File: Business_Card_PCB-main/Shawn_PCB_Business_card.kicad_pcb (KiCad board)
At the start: 2 copper layers, 86.6 x 54.7 mm, 28 parts, among them U1 NT3H1101W0FHKH

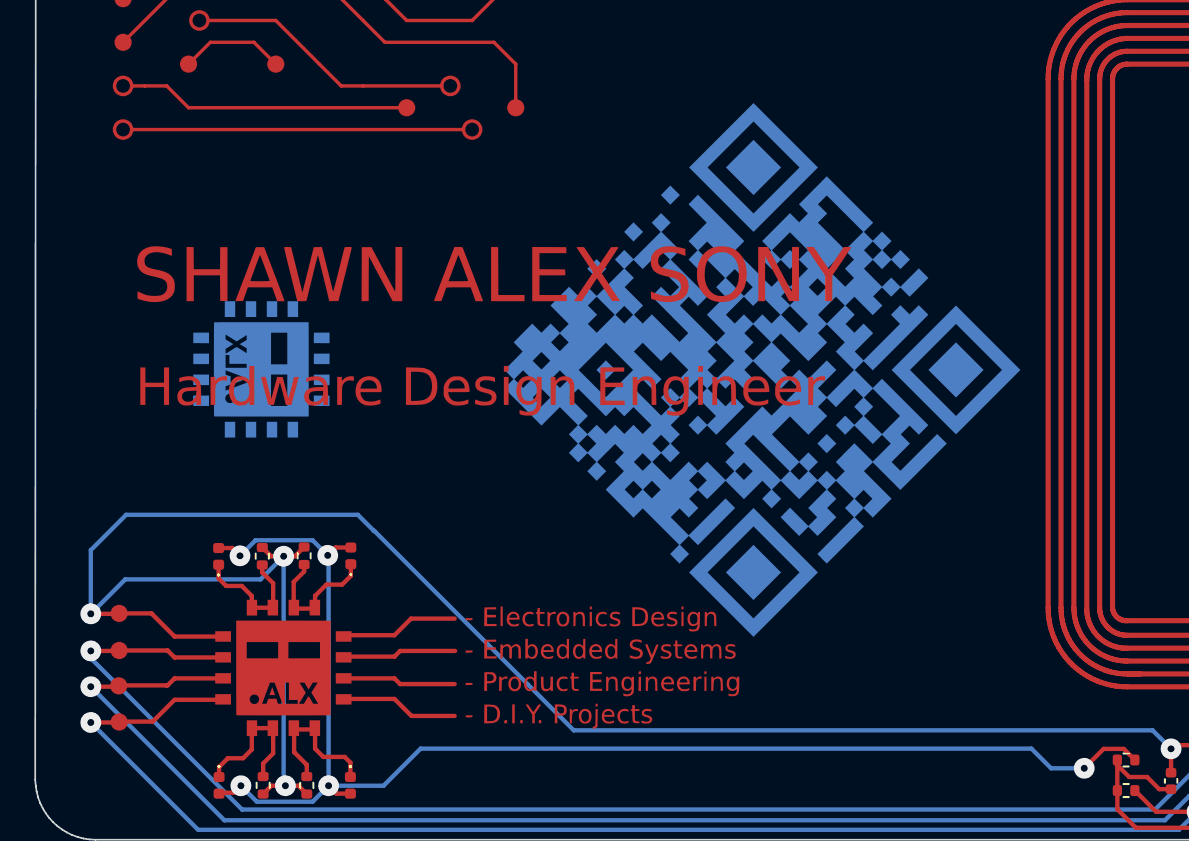
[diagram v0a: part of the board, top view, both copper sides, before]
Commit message: added my name and redesigned the PCB logo thing
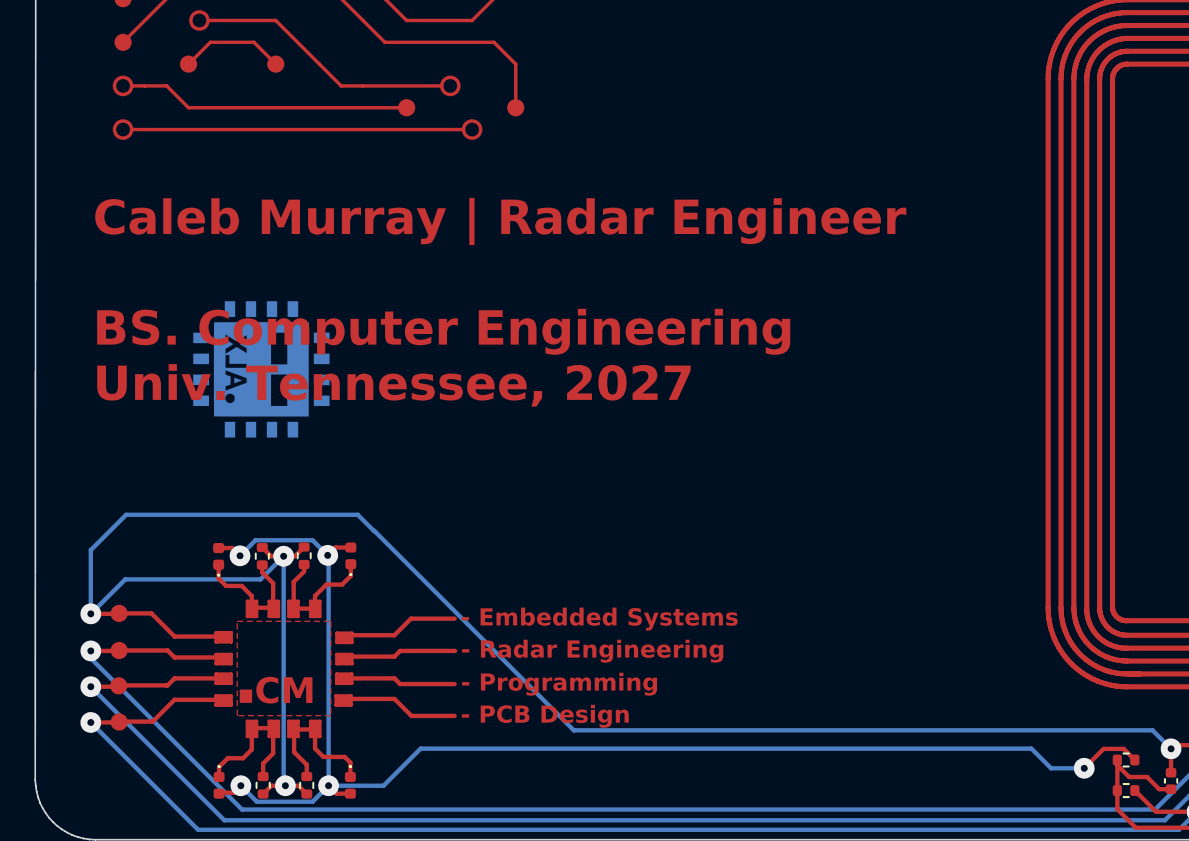
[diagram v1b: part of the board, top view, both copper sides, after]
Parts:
- removed the G*** at (148.2, 69.5) (x2)
- removed the G*** at (148.5, 70.5) (x2)
- removed the G*** at (121.1, 87.9) (x2)
- moved G*** 2.40 mm to (152.0, 71.2)
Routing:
- added copper zone on F.Cu, net (none)
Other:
- board text added: "- Embedded Systems"
- board text added: "- PCB Design"
- board text added: "- Programming"
- board text added: "- Radar Engineering"
- board text added: "."
- board text added: "CM"
- board text added: "Caleb Murray | Radar Engineer BS. Computer Engineering Univ. Tennessee, 2027"

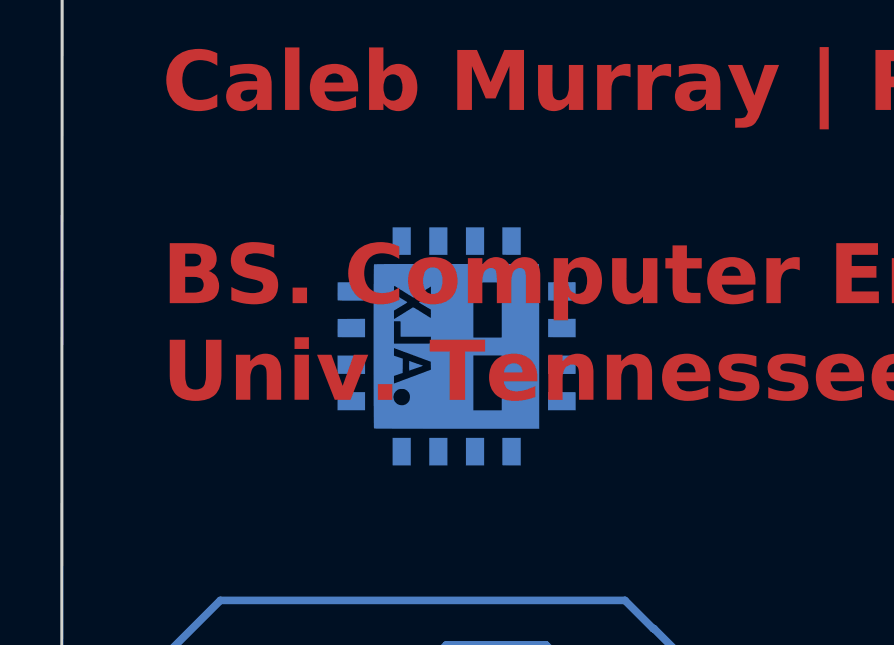
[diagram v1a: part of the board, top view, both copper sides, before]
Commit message: updated back text
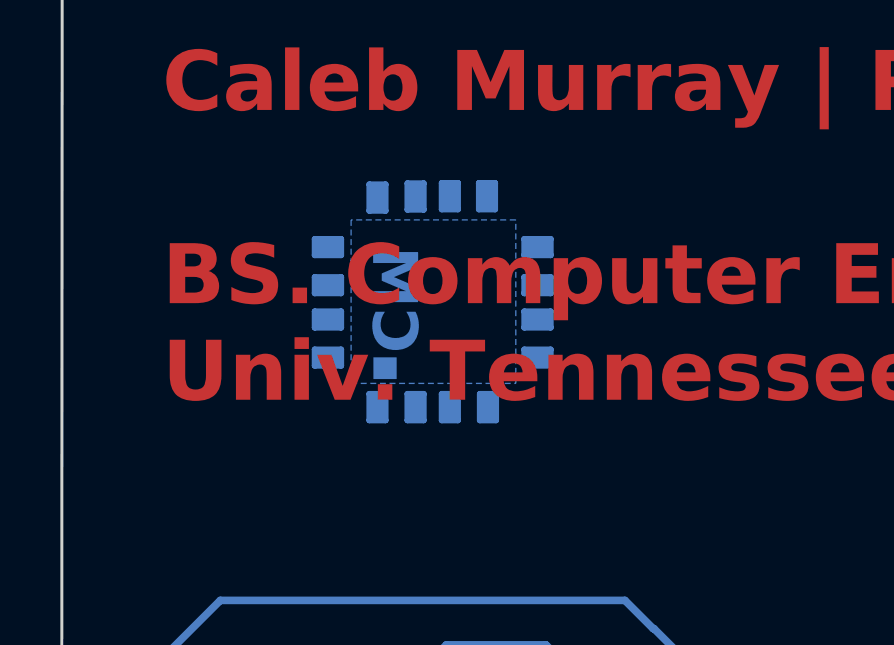
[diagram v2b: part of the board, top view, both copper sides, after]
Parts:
- removed the G*** at (119.8, 70.5) (x2)
- removed the G*** at (152.0, 71.2)
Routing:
- added copper zone on B.Cu, net (none)
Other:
- board text added: "> root@caleb.cm:~$ cat Hello.txt > ----------------------- Hey! I'm Caleb! It's nice to meet you. Scan the card to connect. ----------------------- > root@caleb.cm:~$"

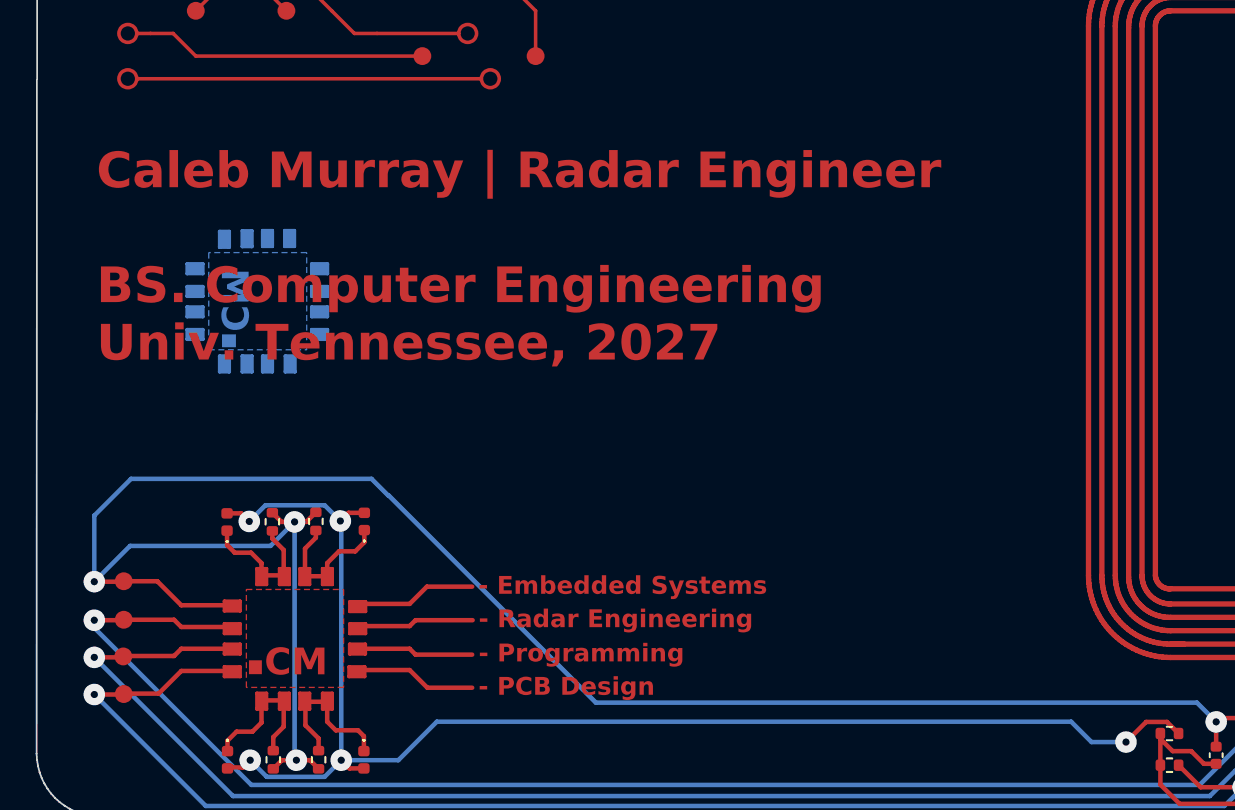
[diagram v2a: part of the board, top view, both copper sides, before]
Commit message: fixed soldermask everywhere
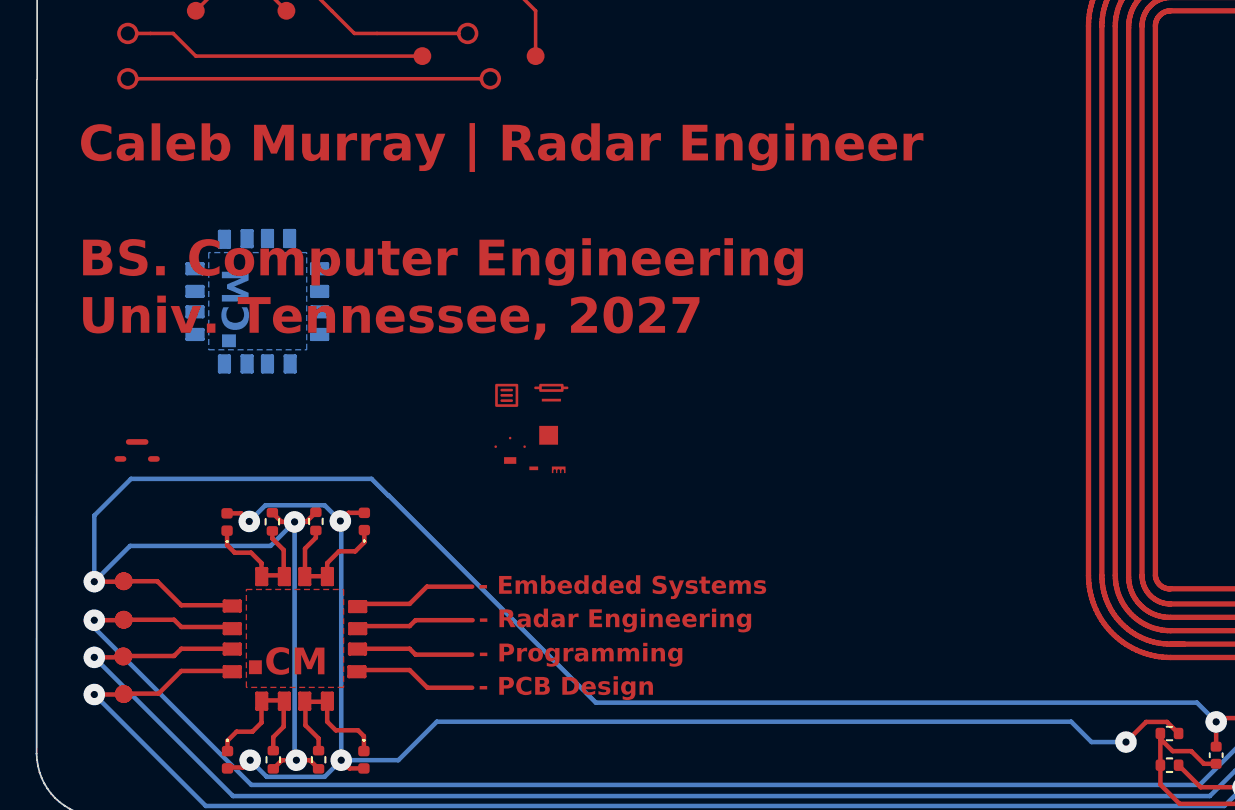
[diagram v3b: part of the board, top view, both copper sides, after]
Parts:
- added TP1: TestPoint, TestPoint:TestPoint_Pad_D1.0mm, F.Cu at (111.5, 86.8)
- added TP2: TestPoint, TestPoint:TestPoint_Pad_D1.0mm, F.Cu at (111.5, 88.9)
- added TP4: TestPoint, TestPoint:TestPoint_Pad_D1.0mm, F.Cu at (111.5, 91.0)
- added TP5: TestPoint, TestPoint:TestPoint_Pad_D1.0mm, F.Cu at (111.5, 84.7)
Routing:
- net (no net): track 26.9 -> 53.8 mm
- net GND: track 119.4 -> 133.6 mm
- net Net-(D1-Pad1): track 8.61 -> 17.2 mm
- net Net-(D2-Pad1): track 8.46 -> 16.9 mm
- net VCC: track 84.2 -> 92.6 mm
- net Net-(D4-Pad1): track 7.97 -> 15.9 mm
- net Net-(TP2-Pad1): track 79.1 -> 87.1 mm
- net Net-(TP1-Pad1): track 79.7 -> 87.6 mm
- net Net-(D3-Pad1): track 7.79 -> 15.6 mm
- net Net-(D1-Pad2): track 80.2 -> 86.0 mm
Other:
- board text added: "42..."
- board text removed: "SCAN HERE"

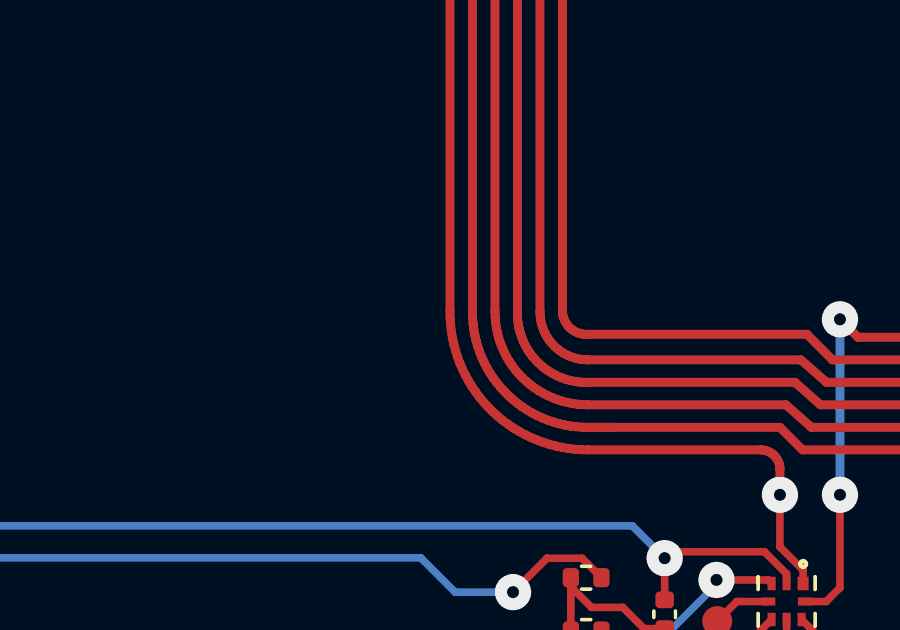
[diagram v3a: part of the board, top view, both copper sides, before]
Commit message: slightly fixed back text. pretty done
thinking about updating comp sizes to 0603
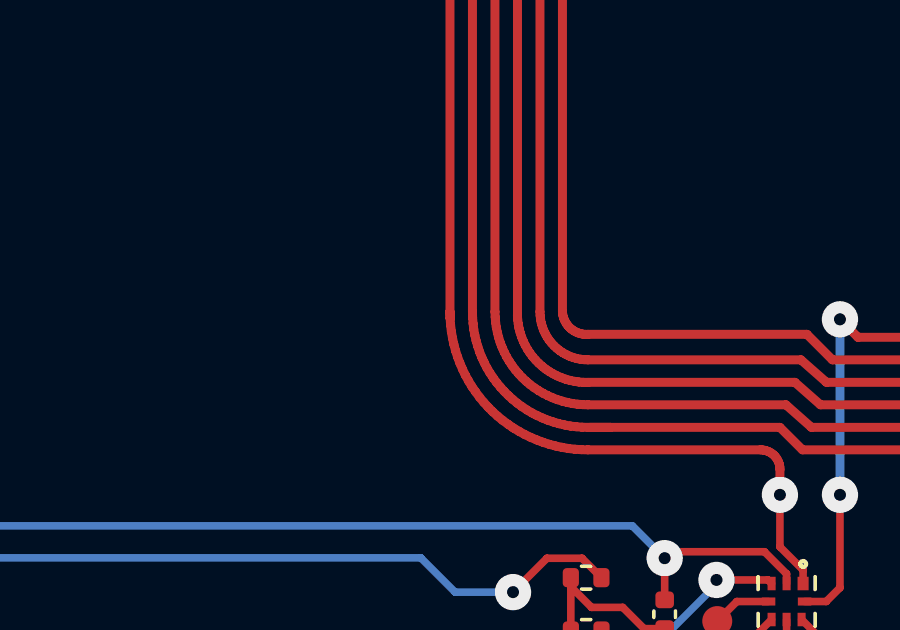
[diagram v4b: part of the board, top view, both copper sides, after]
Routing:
- net Net-(U1-Pad1): track 665.1 -> 1316.7 mm

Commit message: added more text
MS. Electrical Engineering and J in Caleb J. Murray
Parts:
- moved REF** 2.41 mm to (125.7, 55.8)
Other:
- board text added: "Caleb J. Murray | Radar Engineer BS. Computer Engineering MS. Electrical Engineering Univ. Tennessee, 2027"
- board text added: "Caleb J. Murray | Radar Engineer BS. Computer Engineering Univ. Tennessee, 2027"
- board text removed: "Caleb Murray | Radar Engineer BS. Computer Engineering Univ. Tennessee, 2027"

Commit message: fixed some text
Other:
- board text removed: "Caleb J. Murray | Radar Engineer BS. Computer Engineering Univ. Tennessee, 2027"
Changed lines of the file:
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@@
-		)
-	)
-	(gr_text "Caleb J. Murray | Radar Engineer\n\nBS. Computer Engineering\nUniv. Tennessee, 2027"
-		(at 82.7 39.41 0)
-		(layer "F.Cu")
-		(effects
-			(font
-				(size 2 2)
-				(thickness 0.3)
-				(bold yes)
-			)
-			(justify left bottom)
 		)
 	)
@@
 				(bold yes)
 			)
-			(justify left bottom)
-		)
-	)
-	(gr_text "Caleb J. Murray | Radar Engineer\n\nBS. Computer Engineering\nUniv. Tennessee, 2027"
-		(at 82.7 39.41 0)
-		(layer "F.Mask")
-		(effects
-			(font
-				(size 2 2)
-				(thickness 0.3)
-				(bold yes)
-			)

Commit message: added QR code
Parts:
- added G***: LOGO, qr:qrcodefoot, B.Cu at (147.7, 69.3)
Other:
- board text added: "Scan me!"
